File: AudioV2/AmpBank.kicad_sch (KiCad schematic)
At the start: 8 parts

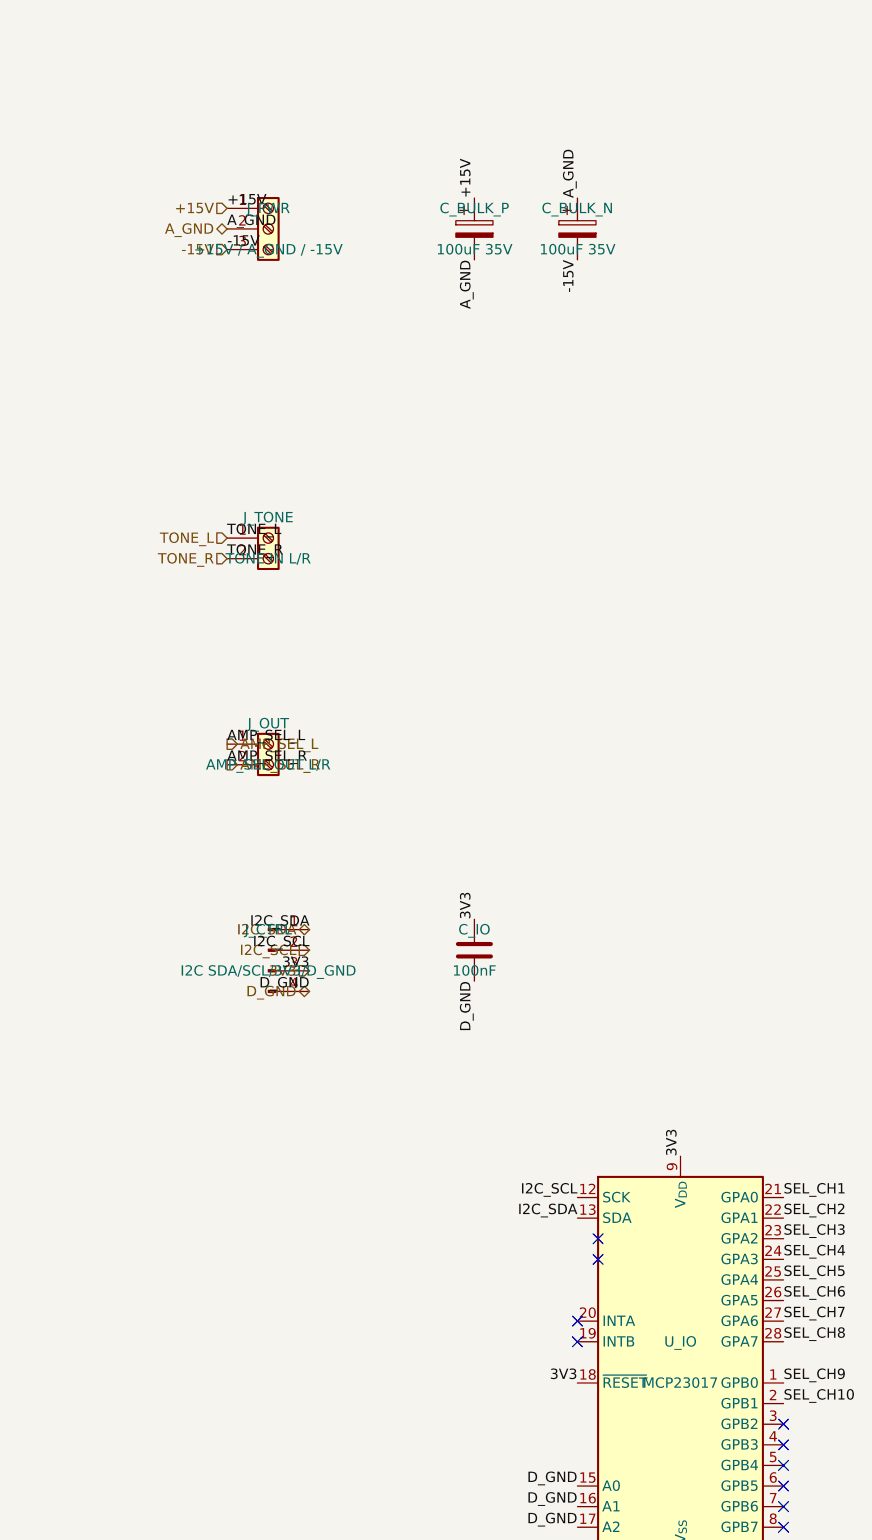
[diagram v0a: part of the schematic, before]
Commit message: AudioV2: AmpCh2手直しに伴う所有権更新、電源コンバータ代替調査、発注リスト追加
AmpBank/AmpChannelはユーザーがKiCadでAmpCh2を手直ししたため生成コード所有
から手編集所有へ卒業（wire_circuit_design.pyのHAND_EDITED/GENERATED更新、
driftで確認）。バルクコンデンサ周りの未接続配線をユーザーが修正、ERC 60件に復帰。

DECISIONS.md §11.1に電流マージンの実測ベース数値根拠を追記（±15V化後の実負荷、
オペアンプ差し替え最悪ケース）。PowerModuleの絶縁型DC-DCコンバータ(DKMW20F-15)
のコスト代替調査を開始し、AGENT_HANDOFF.md §2.10に途中経過と次のアクションを
記録（dc_dc.csvはDigiKeyのフィルタ済みエクスポート）。

AudioV2全体の発注リスト(PROCUREMENT.xlsx)を新規作成。

Co-Authored-By: Claude Sonnet 5 <noreply@anthropic.com>
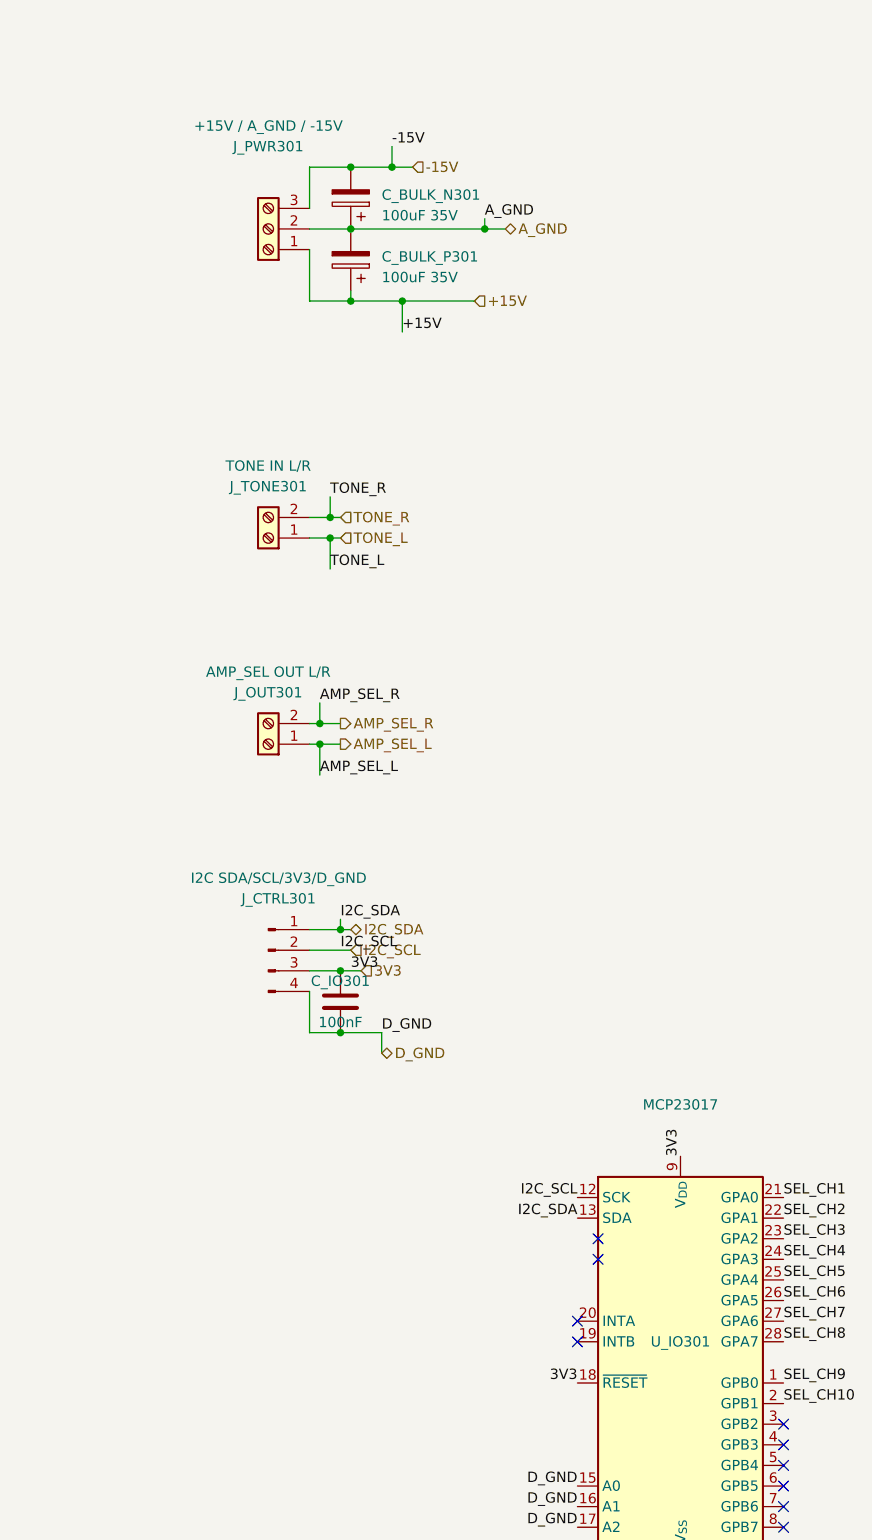
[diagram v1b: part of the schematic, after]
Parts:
- removed C_BULK_N, C_BULK_P: 100uF 35V, Capacitor_SMD:CP_Elec_10x12.6, symbol Device:C_Polarized
- removed C_IO: 100nF, Capacitor_SMD:C_1206_3216Metric_Pad1.33x1.80mm_HandSolder, symbol Device:C
- added C_BULK_N301, C_BULK_P301: 100uF 35V, Capacitor_SMD:CP_Elec_10x12.6, symbol Device:C_Polarized
- added C_IO301: 100nF, Capacitor_SMD:C_1206_3216Metric_Pad1.33x1.80mm_HandSolder, symbol Device:C
- renumbered J_CTRL to J_CTRL301, J_OUT to J_OUT301, J_PWR to J_PWR301, J_TONE to J_TONE301, U_IO to U_IO301
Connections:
- net +15V: now also C_BULK_P301.1
- net -15V: now also C_BULK_N301.2
- net 3V3: now also C_IO301.1
- net A_GND: now also C_BULK_N301.1, C_BULK_P301.2
- net D_GND: now also C_IO301.2
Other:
- moved on the sheet: J_OUT301, J_PWR301, J_TONE301
